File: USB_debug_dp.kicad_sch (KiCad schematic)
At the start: 116 parts, among them J4 USB-C_Amphenol_12401598E4, J4 USB-C_GCT_USB4105-GF-A, Q15 PJE138K, Q3 PJE138K, U11 NCP730BMT330_WSON, U12 NTS0102_XSON, U13 TUSB1046-DCIRNQ, U14 FT230X_QFN, U15 AP22615A_TSOT26, U17 TPD4E05U06QDQARQ1, U18 TPD4E05U06QDQARQ1, U19 TPD4E05U06QDQARQ1, U20 TPD4E05U06QDQARQ1, U8 TPS65988DHRSHR, U9 W25Q80DV_USON

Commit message: [#81970] Finalize connecting SFP+ to SOM
[#82054] Update SoM pins definitions

[#82054] Continue work on I2C

[#82330] Clean up

[#81970] Add SFP sheet and power section

[#82330] Annotation and clean up
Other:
- note added: "USB DP"
- note added: "USB Debug"
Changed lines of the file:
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@@
 		)
 	)
+	(text "USB DP\n"
+		(exclude_from_sim no)
+		(at 194.056 20.32 0)
+		(effects
+			(font
+				(size 2.54 2.54)
+			)
+		)
+	)
+	(text "USB Debug"
+		(exclude_from_sim no)
+		(at 240.284 189.23 0)
+		(effects
+			(font
+				(size 2.54 2.54)
+			)
+		)
+	)
 	(text "H"
 		(exclude_from_sim no)
@@
 		)
 	)
-	(text "I_{LIM}(A) = 6800/R_{LIM} = 3.09\n"
-		(exclude_from_sim no)
-		(at 320.802 171.958 0)
-		(effects
-			(font
-				(size 1.27 1.27)
-			)
-		)
-	)
 	(text "L"
 		(exclude_from_sim no)
@@
 		)
 	)
+	(polyline
+		(pts
+			(xy 11.43 213.36) (xy 101.6 213.36)
+		)
+		(stroke
+			(width 0)
+			(type default)
+		)
+	)
 	(wire
 		(pts
@@
 	(polyline
 		(pts
+			(xy 101.6 184.15) (xy 101.6 213.36)
+		)
+		(stroke
+			(width 0)
+			(type default)
+		)
+	)
+	(polyline
+		(pts
 			(xy 179.07 101.6) (xy 147.32 101.6)
 		)
@@
 		)
 		(stroke
+			(width 0)
+			(type default)
+		)
+	)
+	(polyline
+		(pts
+			(xy 407.67 184.15) (xy 101.6 184.15)
+		)
+		(stroke

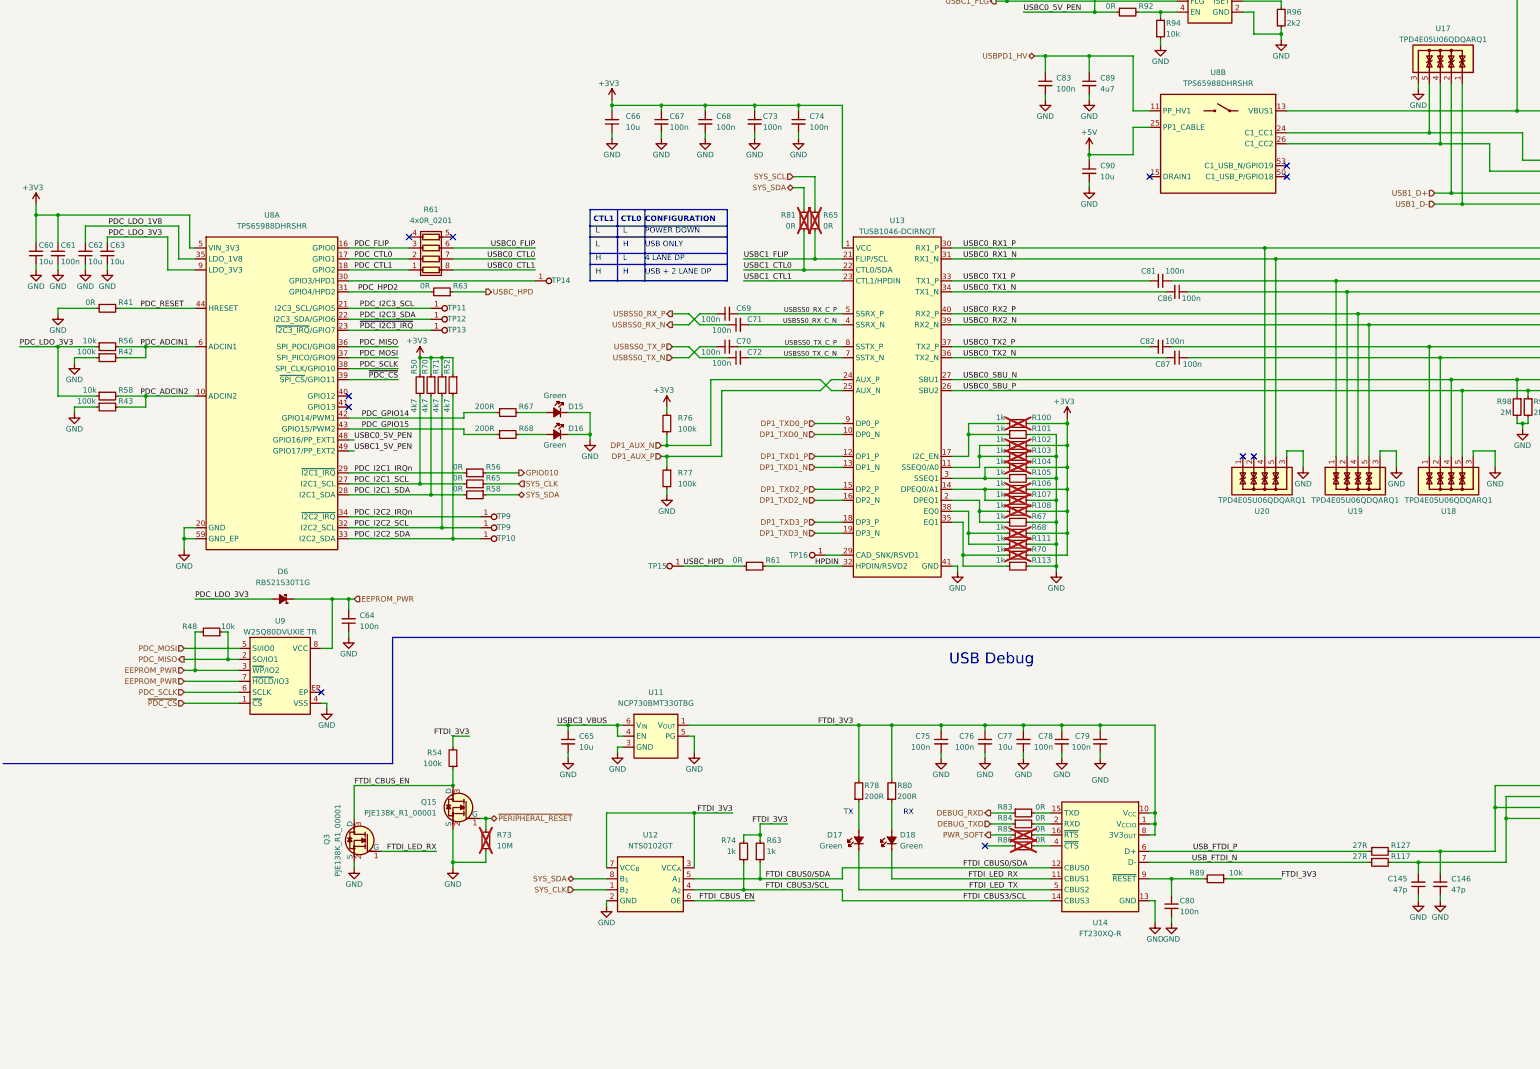
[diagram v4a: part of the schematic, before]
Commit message: [#82330] Add TPM
[#82330] Add ID-EEPROM

[#82055] Clean up
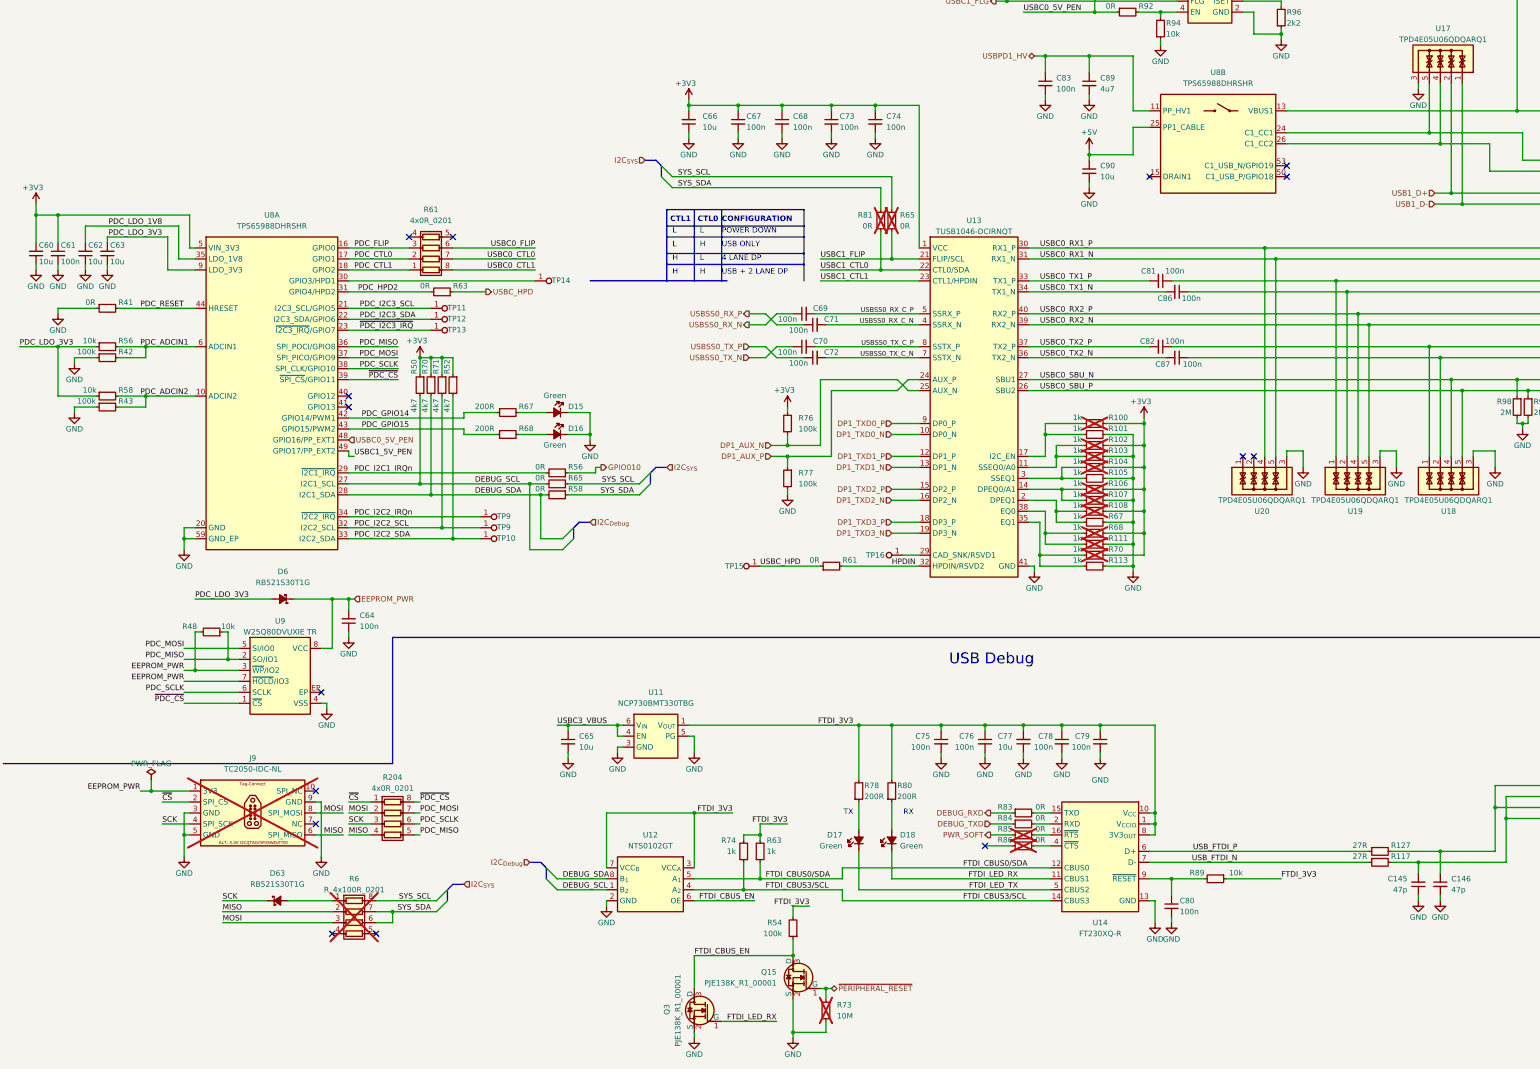
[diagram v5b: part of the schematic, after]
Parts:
- added D63: RB521S30T1G, antmicro-footprints:SOD-523, symbol antmicroDiodesRectifiersSingle:RB521S30T1G
- added J9: Tag-Connect_TC2050-IDC-NL_2x5_P1.27mm, antmicro-footprints:Tag-Connect_TC2050-IDC-NL_2x5_P1.27mm, symbol antmicroTestPoints:Tag-Connect_TC2050-IDC-NL_2x5_P1.27mm
- added R204: R_4x0R_0201_array, antmicro-footprints:R_Array_4x0201_Panasonic_EXB18V, symbol antmicroResistorNetworksArrays:R_4x0R_0201_array
- added R6: R_4x100R_0201_array, antmicro-footprints:R_Array_4x0201_Panasonic_EXB18V, symbol antmicroResistorNetworksArrays:R_4x100R_0201_array
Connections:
- net EEPROM_PWR: now also J9.1
- net GND: now also J9.3, J9.5, J9.9
- net PDC_MISO: now also R204.5 (R4.2)
- net PDC_MOSI: now also R204.7 (R2.2)
- net PDC_SCLK: now also R204.6 (R3.2)
- net SYS_SCL: now also R65.1, R6.8 (R1.2)
- net SYS_SDA: now also R6.6 (R3.2), R6.7 (R2.2); no longer U12.8 (B_{1})
- net ~{PDC_CS}: now also R204.8 (R1.2)
- net PDC_I2C1_SCL renamed DEBUG_SCL
- net DEBUG_SCL: now also U12.1 (B_{2})
- net PDC_I2C1_SDA renamed DEBUG_SDA
- net DEBUG_SDA: now also U12.8 (B_{1})
- removed net SYS_CLK: R65.1, U12.1 (B_{2})
- new net: D63.2 (A), R6.1 (R1.1)
- new net MISO: J9.6, R204.4 (R4.1), R6.2 (R2.1)
- new net MOSI: J9.8, R204.2 (R2.1), R6.3 (R3.1)
- new net SCK: D63.1 (C), J9.4, R204.3 (R3.1)
- new net ~{CS}: J9.2, R204.1 (R1.1)
- no-connect marks 16 -> 20
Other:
- moved on the sheet: C66, C67, C68, C69, C70, C71, C72, C73, C74, Q15, Q3, R100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

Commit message: [#82057] Reorganise FMC+ pins so that they obey standard
[#82057] Add passives to expansion connector

[#82055] Clean up
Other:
- note removed: "USB DP"
- note removed: "USB Debug"
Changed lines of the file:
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@@
 		)
 	)
-	(text "USB DP\n"
-		(exclude_from_sim no)
-		(at 194.056 20.32 0)
-		(effects
-			(font
-				(size 2.54 2.54)
-			)
-		)
-	)
-	(text "USB Debug"
-		(exclude_from_sim no)
-		(at 240.284 189.23 0)
-		(effects
-			(font
-				(size 2.54 2.54)
-			)
-		)
-	)
 	(text "H"
 		(exclude_from_sim no)
@@
 		)
 	)
-	(polyline
-		(pts
-			(xy 11.43 213.36) (xy 101.6 213.36)
-		)
-		(stroke
-			(width 0)
-			(type default)
-		)
-	)
 	(wire
 		(pts
@@
 	(polyline
 		(pts
-			(xy 101.6 184.15) (xy 101.6 213.36)
-		)
-		(stroke
-			(width 0)
-			(type default)
-		)
-	)
-	(polyline
-		(pts
-			(xy 179.07 101.6) (xy 147.32 101.6)
+			(xy 196.85 101.6) (xy 165.1 101.6)
 		)
 		(stroke
@@
 		)
 		(stroke
-			(width 0)
-			(type default)
-		)
-	)
-	(polyline
-		(pts
-			(xy 407.67 184.15) (xy 101.6 184.15)
-		)
-		(stroke

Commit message: [#82055] Fix debug port power
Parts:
- removed C145, C146: C_47p_0402, antmicro-footprints:C_0402_1005Metric, symbol antmicroCapacitors0402:C_47p_0402
- removed C65: C_10u_25V_0603, antmicro-footprints:C_0603_1608Metric, symbol antmicroCapacitors0603:C_10u_25V_0603
- removed C75, C76, C78, C79, C80: C_100n_0402, antmicro-footprints:C_0402_1005Metric, symbol antmicroCapacitors0402:C_100n_0402
- removed C77: C_10u_0402, antmicro-footprints:C_0402_1005Metric, symbol antmicroCapacitors0402:C_10u_0402
- removed D17, D18: LED_G_0603_LTST-C190GKT, antmicro-footprints:LED_0603_1608Metric_G, symbol antmicroLEDIndicationDiscrete:LED_G_0603_LTST-C190GKT
- removed J4: USB-C_GCT_USB4105-GF-A, antmicro-footprints:USB-C_Receptacle_GCT_USB4105-GF-A, symbol antmicroUSBConnectors:USB-C_GCT_USB4105-GF-A
- removed Q15, Q3: PJE138K, antmicro-footprints:SOT-523, symbol antmicroTransistorsFETsMOSFETsSingle:PJE138K
- removed R117, R127: R_27R_0402, antmicro-footprints:R_0402_1005Metric, symbol antmicroResistors0402:R_27R_0402
- removed R54: R_100k_0402, antmicro-footprints:R_0402_1005Metric, symbol antmicroResistors0402:R_100k_0402
- removed R63, R74: R_1k_0402, antmicro-footprints:R_0402_1005Metric, symbol antmicroResistors0402:R_1k_0402
- removed R73: R_10M_0402, antmicro-footprints:R_0402_1005Metric, symbol antmicroResistors0402:R_10M_0402
- removed R78, R80: R_200R_0402, antmicro-footprints:R_0402_1005Metric, symbol antmicroResistors0402:R_200R_0402
- removed R83, R84, R85, R86: R_0R_0402, antmicro-footprints:R_0402_1005Metric, symbol antmicroResistors0402:R_0R_0402
- removed R89: R_10k_0402, antmicro-footprints:R_0402_1005Metric, symbol antmicroResistors0402:R_10k_0402
- removed U11: NCP730BMT330_WSON, antmicro-footprints:WSON-6-1EP_2x2mm_P0.65mm, symbol antmicroPMICVoltageRegulatorsLinear:NCP730BMT330_WSON
- removed U12: NTS0102_XSON, antmicro-footprints:XSON-8_1x1.95mm_P0.5mm, symbol antmicroLogicTranslatorsLevelShifters:NTS0102_XSON
- removed U14: FT230X_QFN, antmicro-footprints:QFN-16-1EP_4x4mm_P0.65mm, symbol antmicroInterfaceControllers:FT230X_QFN
- added C1, C2, C5, C6, C7: C_100n_0402, antmicro-footprints:C_0402_1005Metric, symbol antmicroCapacitors0402:C_100n_0402
- added C3: C_10u_0402, antmicro-footprints:C_0402_1005Metric, symbol antmicroCapacitors0402:C_10u_0402
- added C7: C_10u_25V_0603, antmicro-footprints:C_0603_1608Metric, symbol antmicroCapacitors0603:C_10u_25V_0603
- added C8, C9: C_47p_0402, antmicro-footprints:C_0402_1005Metric, symbol antmicroCapacitors0402:C_47p_0402
- added D1, D2: LED_G_0603_LTST-C190GKT, antmicro-footprints:LED_0603_1608Metric_G, symbol antmicroLEDIndicationDiscrete:LED_G_0603_LTST-C190GKT
- added J3: USB-C_GCT_USB4105-GF-A, antmicro-footprints:USB-C_Receptacle_GCT_USB4105-GF-A, symbol antmicroUSBConnectors:USB-C_GCT_USB4105-GF-A
- added Q2: PJE138K, antmicro-footprints:SOT-523, symbol antmicroTransistorsFETsMOSFETsSingle:PJE138K
- added R10, R11: R_200R_0402, antmicro-footprints:R_0402_1005Metric, symbol antmicroResistors0402:R_200R_0402
- added R12, R13, R14, R15: R_0R_0402, antmicro-footprints:R_0402_1005Metric, symbol antmicroResistors0402:R_0R_0402
- added R16: R_10k_0402, antmicro-footprints:R_0402_1005Metric, symbol antmicroResistors0402:R_10k_0402
- added R17, R18: R_27R_0402, antmicro-footprints:R_0402_1005Metric, symbol antmicroResistors0402:R_27R_0402
- added R19, R20: R_5k1_0402, antmicro-footprints:R_0402_1005Metric, symbol antmicroResistors0402:R_5k1_0402
- added R7, R8: R_1k_0402, antmicro-footprints:R_0402_1005Metric, symbol antmicroResistors0402:R_1k_0402
- added R9: R_100k_0402, antmicro-footprints:R_0402_1005Metric, symbol antmicroResistors0402:R_100k_0402
- added U3: NTS0102_XSON, antmicro-footprints:XSON-8_1x1.95mm_P0.5mm, symbol antmicroLogicTranslatorsLevelShifters:NTS0102_XSON
- added U4: FT230X_QFN, antmicro-footprints:QFN-16-1EP_4x4mm_P0.65mm, symbol antmicroInterfaceControllers:FT230X_QFN
- added U4: NCP730BMT330_WSON, antmicro-footprints:WSON-6-1EP_2x2mm_P0.65mm, symbol antmicroPMICVoltageRegulatorsLinear:NCP730BMT330_WSON
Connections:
- net DEBUG_RXD: now also R12.1
- net DEBUG_SCL: now also U3.1 (B_{2})
- net DEBUG_SDA: now also U3.8 (B_{1})
- net DEBUG_TXD: now also R13.1
- net FTDI_3V3: now also C1.1, C2.1, C3.2, C5.1, C6.1, R10.2, R11.2, R16.1, R7.2, R8.2, R9.2, U3.3 (VCC_{A}), U3.7 (VCC_{B}), U4.1 (V_{CCIO}), U4.1 (V_{OUT}), U4.10 (V_{CC}), U4.8 (3V3_{OUT})
- net FTDI_CBUS0/SDA: now also R8.1, U3.5 (A_{1}), U4.12 (CBUS0)
- net FTDI_CBUS3/SCL: now also R7.1, U3.4 (A_{2}), U4.14 (CBUS3)
- net FTDI_CBUS_EN: now also Q2.3 (D), R9.1, U3.6 (OE)
- net FTDI_LED_RX: now also D2.1 (C), Q2.1 (G), U4.11 (CBUS1)
- net FTDI_LED_TX: now also D1.1 (C), U4.5 (CBUS2)
- net GND: now also C1.2, C2.2, C3.1, C5.2, C6.2, C7.2, C7.2, C8.1, C9.2, J3.A1 (GND), J3.A12 (GND), J3.B1 (GND), J3.B12 (GND), J3.SH, Q2.2 (S), R19.1, R20.1, U3.2 (GND), U4.13 (GND), U4.17 (GND), U4.3 (GND), U4.3 (GND), U4.5 (PG), U4.7 (GND)
- net PWR_SOFT: now also R14.1
- net USB_FTDI_N: now also R18.1, U4.7 (D-)
- net USB_FTDI_P: now also R17.1, U4.6 (D+)
- new net: D2.2 (A), R11.1
- new net: C8.2, J3.A7 (D_{A}-), J3.B7 (D_{B}-), R18.2
- new net: J3.B5 (CC_{2}), R20.2
- new net: C7.1, U4.4 (EN), U4.6 (V_{IN})
- new net: R13.2, U4.2 (RXD)
- new net: D1.2 (A), R10.1
- new net: C9.1, J3.A6 (D_{A}+), J3.B6 (D_{B}+), R17.2
- new net: J3.A4 (VBUS), J3.A9 (VBUS), J3.B4 (VBUS), J3.B9 (VBUS)
- new net: J3.A5 (CC_{1}), R19.2
- new net: R12.2, U4.15 (TXD)
- new net: R14.2, U4.16 (~{RTS})
- new net: R15.2, U4.4 (~{CTS})
- new net: C7.1, R16.2, U4.9 (~{RESET})
- no-connect marks 20 -> 17
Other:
- note added: "USB Debug"
- note added: "USB Display port alt mode"
- note added: "USB PD controller"
- moved on the sheet: C64, D6, D63, J9, R204, R48, R6, U9
